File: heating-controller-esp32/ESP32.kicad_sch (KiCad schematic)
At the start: 29 parts, among them J1 431151015826, J2 431151015826, Q1 MBT3904DW1, U1 ESP32-WROOM-32U, U2 CP2102N-A01-GQFN28

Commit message: Initial design of schematic complete. Started laying out PCB
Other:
- note added: "Voltage divider, see p.20 https://www.silabs.com/documents/public/data-sheets/CP2102-9.pdf"
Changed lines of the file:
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@@
   (junction (at 175.26 86.36) (diameter 0) (color 0 0 0 0)
   )
+  (junction (at 187.96 66.04) (diameter 0) (color 0 0 0 0)
+  )
   (junction (at 168.91 148.59) (diameter 0) (color 0 0 0 0)
   )
+  (junction (at 187.96 86.36) (diameter 0) (color 0 0 0 0)
+  )
   (junction (at 130.81 52.07) (diameter 0) (color 0 0 0 0)
   )
+  (junction (at 66.04 59.69) (diameter 0) (color 0 0 0 0)
+  )
+  (junction (at 74.93 57.15) (diameter 0) (color 0 0 0 0)
+  )
   (junction (at 138.43 52.07) (diameter 0) (color 0 0 0 0)
   )
-  (junction (at 66.04 59.69) (diameter 0) (color 0 0 0 0)
-  )
-  (junction (at 74.93 57.15) (diameter 0) (color 0 0 0 0)
-  )
   (junction (at 223.52 29.21) (diameter 0) (color 0 0 0 0)
   )
   (junction (at 139.7 168.91) (diameter 0) (color 0 0 0 0)
+  )
+  (junction (at 156.21 52.07) (diameter 0) (color 0 0 0 0)
   )
   (junction (at 213.36 85.09) (diameter 0) (color 0 0 0 0)
@@
     (stroke (width 0) (type default) (color 0 0 0 0))
   )
-  (wire (pts (xy 186.69 86.36) (xy 175.26 86.36))
+  (wire (pts (xy 175.26 86.36) (xy 187.96 86.36))
     (stroke (width 0) (type default) (color 0 0 0 0))
   )
@@
     (stroke (width 0) (type default) (color 0 0 0 0))
   )
+  (wire (pts (xy 187.96 86.36) (xy 187.96 97.79))
+    (stroke (width 0) (type default) (color 0 0 0 0))
+  )
+  (wire (pts (xy 187.96 66.04) (xy 210.82 66.04))
+    (stroke (width 0) (type default) (color 0 0 0 0))
+  )
   (wire (pts (xy 66.04 62.23) (xy 66.04 59.69))
     (stroke (width 0) (type default) (color 0 0 0 0))
@@
     (stroke (width 0) (type default) (color 0 0 0 0))
   )
+  (wire (pts (xy 187.96 66.04) (xy 187.96 86.36))
+    (stroke (width 0) (type default) (color 0 0 0 0))
+  )
   (wire (pts (xy 226.06 109.22) (xy 243.84 109.22))
     (stroke (width 0) (type default) (color 0 0 0 0))
@@
     (stroke (width 0) (type default) (color 0 0 0 0))
   )
-  (wire (pts (xy 186.69 97.79) (xy 186.69 86.36))
-    (stroke (width 0) (type default) (color 0 0 0 0))
-  )
   (wire (pts (xy 210.82 85.09) (xy 213.36 85.09))
     (stroke (width 0) (type default) (color 0 0 0 0))
@@
     (stroke (width 0) (type default) (color 0 0 0 0))
   )
+  (wire (pts (xy 210.82 85.09) (xy 210.82 97.79))
+    (stroke (width 0) (type default) (color 0 0 0 0))
+  )
+  (wire (pts (xy 190.5 114.3) (xy 200.66 114.3))
+    (stroke (width 0) (type default) (color 0 0 0 0))
+  )
+  (wire (pts (xy 187.96 29.21) (xy 187.96 31.75))
+    (stroke (width 0) (type default) (color 0 0 0 0))
+  )
+  (wire (pts (xy 80.01 127) (xy 80.01 138.43))
+    (stroke (width 0) (type default) (color 0 0 0 0))
+  )
+  (wire (pts (xy 187.96 52.07) (xy 187.96 66.04))
+    (stroke (width 0) (type default) (color 0 0 0 0))
+  )
+  (wire (pts (xy 149.86 130.81) (xy 153.67 130.81))
+    (stroke (width 0) (type default) (color 0 0 0 0))
+  )
+  (wire (pts (xy 187.96 97.79) (xy 210.82 97.79))
+    (stroke (width 0) (type default) (color 0 0 0 0))
+  )
+  (wire (pts (xy 224.79 85.09) (xy 213.36 85.09))
+    (stroke (width 0) (type default) (color 0 0 0 0))
+  )
+  (wire (pts (xy 238.76 85.09) (xy 224.79 85.09))
+    (stroke (width 0) (type default) (color 0 0 0 0))
+  )
+  (wire (pts (xy 72.39 59.69) (xy 72.39 57.15))
+    (stroke (width 0) (type default) (color 0 0 0 0))
+  )
+  (wire (pts (xy 82.55 123.19) (xy 80.01 123.19))
+    (stroke (width 0) (type default) (color 0 0 0 0))
+  )
+  (wire (pts (xy 194.31 116.84) (xy 200.66 116.84))
+    (stroke (width 0) (type default) (color 0 0 0 0))
+  )
+  (wire (pts (xy 151.13 173.99) (xy 195.58 173.99))
+    (stroke (width 0) (type default) (color 0 0 0 0))
+  )
+  (wire (pts (xy 137.16 173.99) (xy 143.51 173.99))
+    (stroke (width 0) (type default) (color 0 0 0 0))
+  )
+  (wire (pts (xy 35.56 59.69) (xy 35.56 62.23))
+    (stroke (width 0) (type default) (color 0 0 0 0))
+  )
+  (wire (pts (xy 74.93 54.61) (xy 74.93 57.15))
+    (stroke (width 0) (type default) (color 0 0 0 0))
+  )
+  (wire (pts (xy 64.77 133.35) (xy 64.77 130.81))
+    (stroke (width 0) (type default) (color 0 0 0 0))
+  )
+  (wire (pts (xy 223.52 29.21) (xy 218.44 29.21))
+    (stroke (width 0) (type default) (color 0 0 0 0))
+  )
+  (wire (pts (xy 74.93 57.15) (xy 77.47 57.15))
+    (stroke (width 0) (type default) (color 0 0 0 0))
+  )
+  (wire (pts (xy 165.1 86.36) (xy 165.1 87.63))
+    (stroke (width 0) (type default) (color 0 0 0 0))
+  )
+  (wire (pts (xy 64.77 130.81) (xy 82.55 130.81))
+    (stroke (width 0) (type default) (color 0 0 0 0))
+  )
+  (wire (pts (xy 118.11 52.07) (xy 118.11 69.85))
+    (stroke (width 0) (type default) (color 0 0 0 0))
+  )
+  (wire (pts (xy 137.16 168.91) (xy 139.7 168.91))
+    (stroke (width 0) (type default) (color 0 0 0 0))
+  )
+  (wire (pts (xy 80.01 123.19) (xy 80.01 121.92))
+    (stroke (width 0) (type default) (color 0 0 0 0))
+  )
+  (wire (pts (xy 139.7 168.91) (xy 139.7 181.61))
+    (stroke (width 0) (type default) (color 0 0 0 0))
+  )
+  (wire (pts (xy 35.56 62.23) (xy 66.04 62.23))
+    (stroke (width 0) (type default) (color 0 0 0 0))
+  )
+  (wire (pts (xy 133.35 133.35) (xy 153.67 133.35))
+    (stroke (width 0) (type default) (color 0 0 0 0))
+  )
   (wire (pts (xy 138.43 52.07) (xy 156.21 52.07))
     (stroke (width 0) (type default) (color 0 0 0 0))
   )
-  (wire (pts (xy 210.82 85.09) (xy 210.82 97.79))
-    (stroke (width 0) (type default) (color 0 0 0 0))
-  )
-  (wire (pts (xy 190.5 114.3) (xy 200.66 114.3))
-    (stroke (width 0) (type default) (color 0 0 0 0))
-  )
-  (wire (pts (xy 187.96 29.21) (xy 187.96 31.75))
-    (stroke (width 0) (type default) (color 0 0 0 0))
-  )
-  (wire (pts (xy 80.01 127) (xy 80.01 138.43))
-    (stroke (width 0) (type default) (color 0 0 0 0))
-  )
-  (wire (pts (xy 149.86 130.81) (xy 153.67 130.81))
-    (stroke (width 0) (type default) (color 0 0 0 0))
-  )
-  (wire (pts (xy 224.79 85.09) (xy 213.36 85.09))
-    (stroke (width 0) (type default) (color 0 0 0 0))
-  )
-  (wire (pts (xy 238.76 85.09) (xy 224.79 85.09))
-    (stroke (width 0) (type default) (color 0 0 0 0))
-  )
-  (wire (pts (xy 72.39 59.69) (xy 72.39 57.15))
-    (stroke (width 0) (type default) (color 0 0 0 0))
-  )
-  (wire (pts (xy 82.55 123.19) (xy 80.01 123.19))
-    (stroke (width 0) (type default) (color 0 0 0 0))
-  )
-  (wire (pts (xy 194.31 116.84) (xy 200.66 116.84))
-    (stroke (width 0) (type default) (color 0 0 0 0))
-  )
-  (wire (pts (xy 151.13 173.99) (xy 195.58 173.99))
-    (stroke (width 0) (type default) (color 0 0 0 0))
-  )
-  (wire (pts (xy 137.16 173.99) (xy 143.51 173.99))
-    (stroke (width 0) (type default) (color 0 0 0 0))
-  )
-  (wire (pts (xy 35.56 59.69) (xy 35.56 62.23))
-    (stroke (width 0) (type default) (color 0 0 0 0))
-  )
-  (wire (pts (xy 74.93 54.61) (xy 74.93 57.15))
-    (stroke (width 0) (type default) (color 0 0 0 0))
-  )
-  (wire (pts (xy 64.77 133.35) (xy 64.77 130.81))
-    (stroke (width 0) (type default) (color 0 0 0 0))
-  )
-  (wire (pts (xy 223.52 29.21) (xy 218.44 29.21))
-    (stroke (width 0) (type default) (color 0 0 0 0))
-  )
-  (wire (pts (xy 74.93 57.15) (xy 77.47 57.15))
-    (stroke (width 0) (type default) (color 0 0 0 0))
-  )
-  (wire (pts (xy 165.1 86.36) (xy 165.1 87.63))
-    (stroke (width 0) (type default) (color 0 0 0 0))
-  )
-  (wire (pts (xy 64.77 130.81) (xy 82.55 130.81))
-    (stroke (width 0) (type default) (color 0 0 0 0))
-  )
-  (wire (pts (xy 118.11 52.07) (xy 118.11 69.85))
-    (stroke (width 0) (type default) (color 0 0 0 0))
-  )
-  (wire (pts (xy 137.16 168.91) (xy 139.7 168.91))
-    (stroke (width 0) (type default) (color 0 0 0 0))
-  )
-  (wire (pts (xy 80.01 123.19) (xy 80.01 121.92))
-    (stroke (width 0) (type default) (color 0 0 0 0))
-  )
-  (wire (pts (xy 139.7 168.91) (xy 139.7 181.61))
-    (stroke (width 0) (type default) (color 0 0 0 0))
-  )
-  (wire (pts (xy 35.56 62.23) (xy 66.04 62.23))
-    (stroke (width 0) (type default) (color 0 0 0 0))
-  )
-  (wire (pts (xy 133.35 133.35) (xy 153.67 133.35))
-    (stroke (width 0) (type default) (color 0 0 0 0))
-  )
   (wire (pts (xy 66.04 59.69) (xy 72.39 59.69))
     (stroke (width 0) (type default) (color 0 0 0 0))
@@
     (stroke (width 0) (type default) (color 0 0 0 0))
   )
-  (wire (pts (xy 186.69 97.79) (xy 210.82 97.79))
-    (stroke (width 0) (type default) (color 0 0 0 0))
-  )
   (wire (pts (xy 200.66 119.38) (xy 195.58 119.38))
     (stroke (width 0) (type default) (color 0 0 0 0))
   )
+  (wire (pts (xy 156.21 52.07) (xy 187.96 52.07))
+    (stroke (width 0) (type default) (color 0 0 0 0))
+  )
   (wire (pts (xy 194.31 171.45) (xy 194.31 116.84))
     (stroke (width 0) (type default) (color 0 0 0 0))
@@
   (wire (pts (xy 137.16 171.45) (xy 143.51 171.45))
     (stroke (width 0) (type default) (color 0 0 0 0))
+  )
+  (text "Voltage divider, see p.20\nhttps://www.silabs.com/documents/public/data-sheets/CP2102-9.pdf"
+    (at 182.88 180.34 0)
+    (effects (font (size 1.27 1.27)) (justify left bottom))
   )
   (text "IO34 and IO35 are \nINPUT only!!!" (at 106.68 130.81 0)
@@
     (effects (font (size 1.27 1.27)) (justify left))
   )
-  (hierarchical_label "ESP_VDD" (shape input) (at 203.2 97.79 90)
+  (hierarchical_label "ESP_VDD" (shape input) (at 210.82 66.04 0)
     (effects (font (size 1.27 1.27)) (justify left))
   )
@@
     (effects (font (size 1.27 1.27)) (justify left))
   )
-  (hierarchical_label "ESP_VDD" (shape input) (at 156.21 52.07 90)
-    (effects (font (size 1.27 1.27)) (justify left))
-  )

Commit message: Changed to Wago connectors; initial routing completed
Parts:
- U1: footprint RF_Module:ESP32-WROOM-32U -> RF_Module:ESP32-WROOM-32
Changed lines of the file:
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@@
     (property "Reference" "U1" (id 0) (at 118.11 65.2526 0))
     (property "Value" "ESP32-WROOM-32U" (id 1) (at 118.11 67.564 0))
-    (property "Footprint" "RF_Module:ESP32-WROOM-32U" (id 2) (at 118.11 143.51 0)
+    (property "Footprint" "RF_Module:ESP32-WROOM-32" (id 2) (at 118.11 143.51 0)
       (effects (font (size 1.27 1.27)) hide)
     )

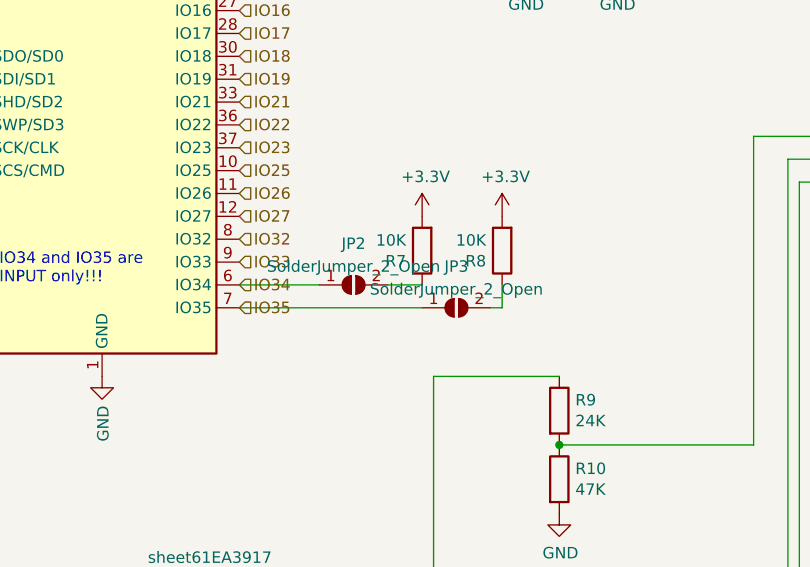
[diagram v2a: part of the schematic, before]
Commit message: Added additional spare thermostat inputs
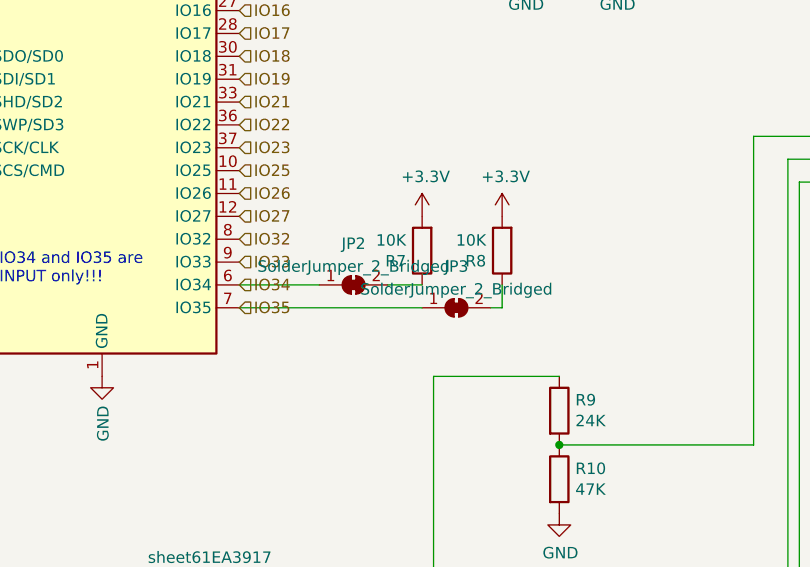
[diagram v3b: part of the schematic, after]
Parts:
- JP2: value SolderJumper_2_Open -> SolderJumper_2_Bridged; symbol Jumper:SolderJumper_2_Open -> Jumper:SolderJumper_2_Bridged
- JP3: value SolderJumper_2_Open -> SolderJumper_2_Bridged; footprint Jumper:SolderJumper-2_P1.3mm_Open_RoundedPad1.0x1.5mm -> Jumper:SolderJumper-2_P1.3mm_Bridged_RoundedPad1.0x1.5mm; symbol Jumper:SolderJumper_2_Open -> Jumper:SolderJumper_2_Bridged
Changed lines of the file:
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@@
     (pin "2")
   )
-  (symbol (lib_id "Jumper:SolderJumper_2_Open") (at 157.48 133.35 0) (unit 1)
+  (symbol (lib_id "Jumper:SolderJumper_2_Bridged") (at 157.48 133.35 0) (unit 1)
     (in_bom yes) (on_board yes) (fields_autoplaced)
     (property "Reference" "JP3" (id 0) (at 157.48 128.7612 0))
-    (property "Value" "SolderJumper_2_Open" (id 1) (at 157.48 131.2981 0))
-    (property "Footprint" "Jumper:SolderJumper-2_P1.3mm_Open_RoundedPad1.0x1.5mm" (id 2) (at 157.48 133.35 0)
+    (property "Value" "SolderJumper_2_Bridged" (id 1) (at 157.48 131.2981 0))
+    (property "Footprint" "Jumper:SolderJumper-2_P1.3mm_Bridged_RoundedPad1.0x1.5mm" (id 2) (at 157.48 133.35 0)
       (effects (font (size 1.27 1.27)) hide)
     )
@@
     (pin "2")
   )
-  (symbol (lib_id "Jumper:SolderJumper_2_Open") (at 146.05 130.81 0) (unit 1)
+  (symbol (lib_id "Jumper:SolderJumper_2_Bridged") (at 146.05 130.81 0) (unit 1)
     (in_bom yes) (on_board yes) (fields_autoplaced)
     (property "Reference" "JP2" (id 0) (at 146.05 126.2212 0))
-    (property "Value" "SolderJumper_2_Open" (id 1) (at 146.05 128.7581 0))
+    (property "Value" "SolderJumper_2_Bridged" (id 1) (at 146.05 128.7581 0))
     (property "Footprint" "Jumper:SolderJumper-2_P1.3mm_Open_RoundedPad1.0x1.5mm" (id 2) (at 146.05 130.81 0)
       (effects (font (size 1.27 1.27)) hide)

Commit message: Mounting holes, a few more tweaks
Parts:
- Q1: LCSC C110150 -> C896759
- Q1: LCSC (none) -> C896759
- U1: LCSC C529580 -> C82899
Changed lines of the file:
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@@
       (effects (font (size 1.27 1.27)) hide)
     )
-    (property "LCSC" "C529580" (id 4) (at 118.11 105.41 0)
+    (property "LCSC" "C82899" (id 4) (at 118.11 105.41 0)
       (effects (font (size 1.27 1.27)) hide)
     )
@@
       (effects (font (size 1.27 1.27)) hide)
     )
-    (property "LCSC" "C110150" (id 4) (at 67.31 121.92 0)
+    (property "LCSC" "C896759" (id 4) (at 67.31 121.92 0)
       (effects (font (size 1.27 1.27)) hide)
     )
@@
       (effects (font (size 1.27 1.27)) hide)
     )
+    (property "LCSC" "C896759" (id 4) (at 67.31 138.43 0)
+      (effects (font (size 1.27 1.27)) hide)
+    )
